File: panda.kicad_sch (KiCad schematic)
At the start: 14 parts

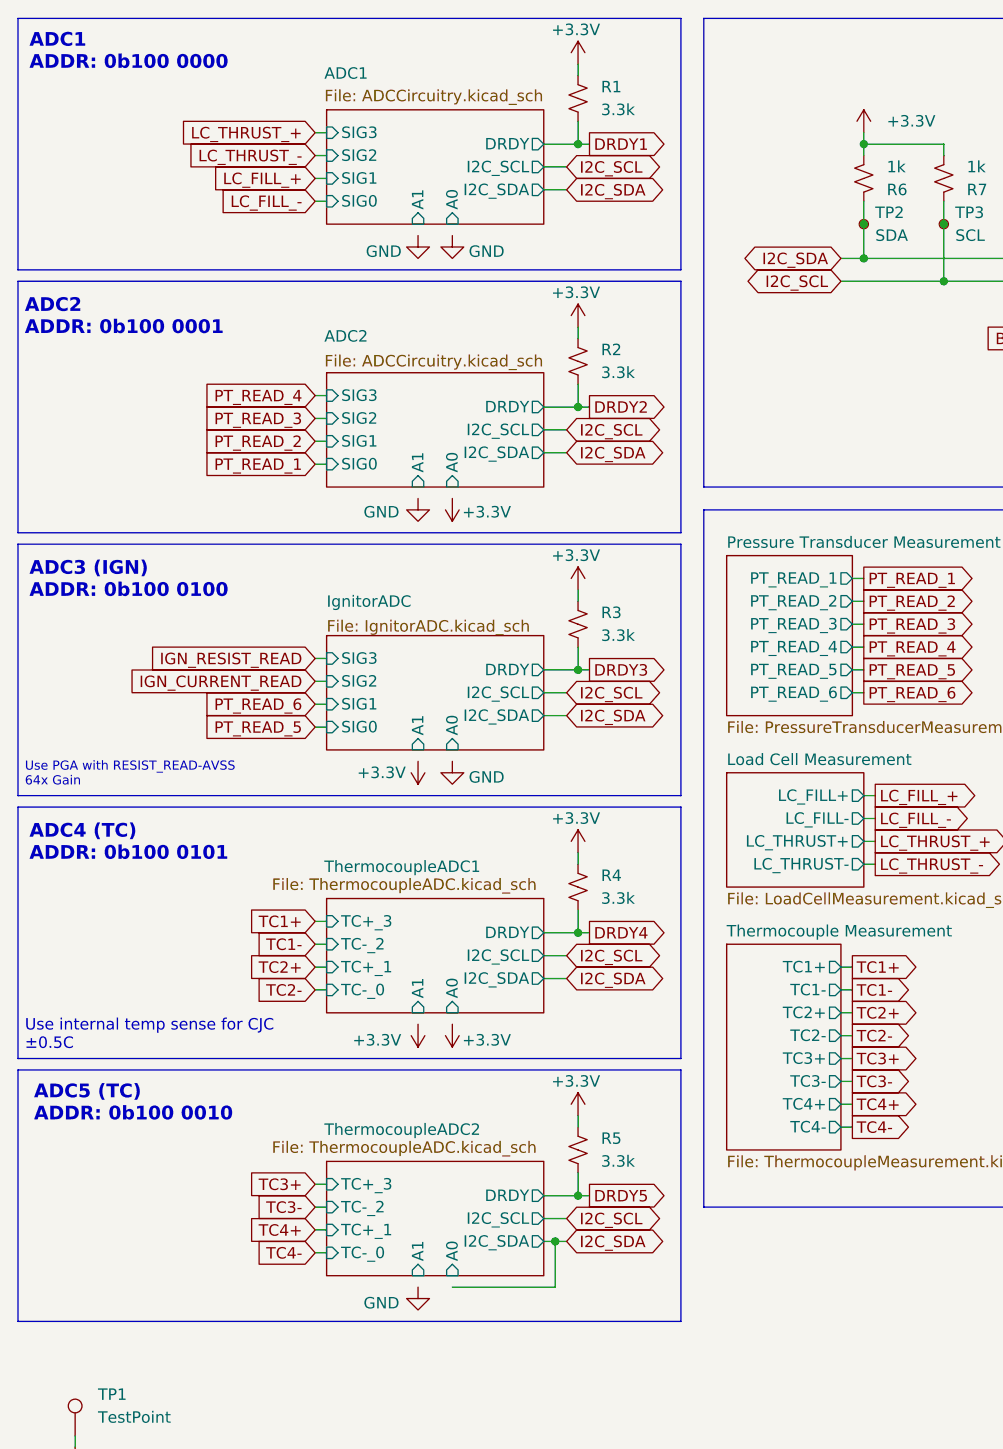
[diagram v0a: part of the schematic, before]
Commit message: change clamping resistors on tc adcs for lower leakage current
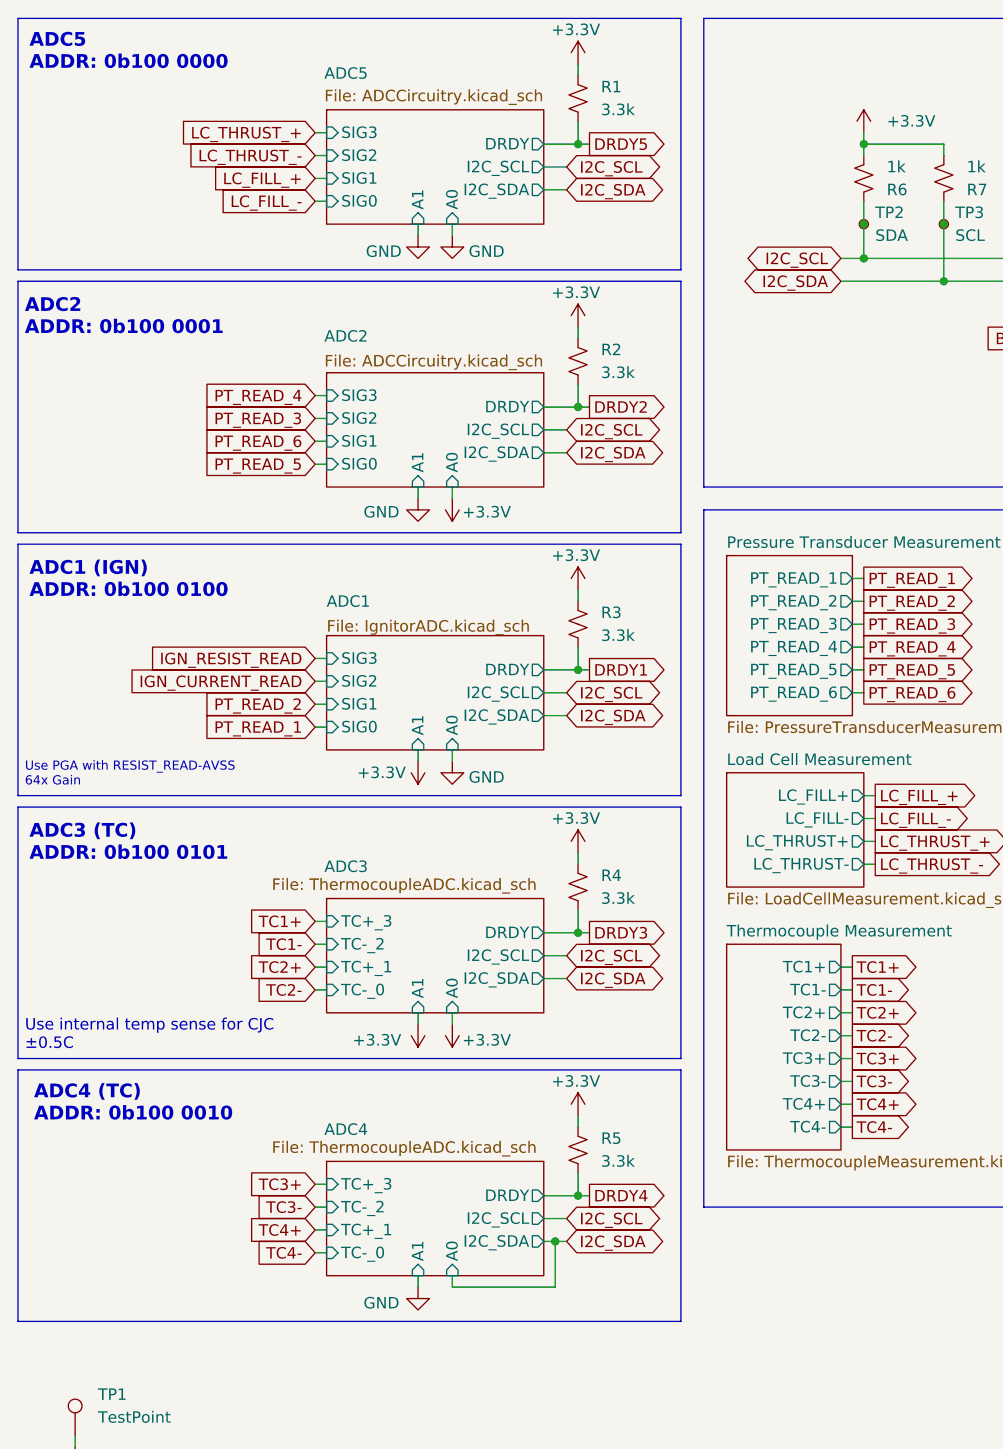
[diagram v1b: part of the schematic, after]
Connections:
- net DRDY1: now also R3.2; no longer R1.2
- net DRDY3: now also R4.2; no longer R3.2
- net DRDY4: now also R5.2; no longer R4.2
- net DRDY5: now also R1.2; no longer R5.2
- net I2C_SCL: now also R6.1, TP2.1; no longer R7.1, TP3.1
- net I2C_SDA: now also R7.1, TP3.1; no longer R6.1, TP2.1
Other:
- sheet ThermocoupleADC1 renamed ADC3
- sheet ThermocoupleADC2 renamed ADC4
- removed sheet IgnitorADC
- added sheet ADC5 (ADCCircuitry.kicad_sch)
- sheet ADC1: file ADCCircuitry.kicad_sch -> IgnitorADC.kicad_sch
- note added: "ADC1 (IGN) ADDR: 0b100 0100"
- note added: "ADC3 (TC) ADDR: 0b100 0101"
- note added: "ADC4 (TC) ADDR: 0b100 0010"
- note added: "ADC5 ADDR: 0b100 0000"
- note removed: "ADC1 ADDR: 0b100 0000"
- note removed: "ADC3 (IGN) ADDR: 0b100 0100"
- note removed: "ADC4 (TC) ADDR: 0b100 0101"
- note removed: "ADC5 (TC) ADDR: 0b100 0010"
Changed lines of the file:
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@@
 		)
 	)
-	(text "ADC3 (IGN)\nADDR: 0b100 0100"
+	(text "ADC1 (IGN)\nADDR: 0b100 0100"
 		(exclude_from_sim no)
 		(at 15.24 76.454 0)
@@
 		)
 	)
-	(text "ADC1\nADDR: 0b100 0000"
+	(text "ADC5\nADDR: 0b100 0000"
 		(exclude_from_sim no)
 		(at 15.24 17.78 0)
@@
 		)
 	)
-	(text "ADC5 (TC)\nADDR: 0b100 0010"
+	(text "ADC4 (TC)\nADDR: 0b100 0010"
 		(exclude_from_sim no)
 		(at 15.748 134.62 0)
@@
 		)
 	)
-	(text "ADC4 (TC)\nADDR: 0b100 0101"
+	(text "ADC3 (TC)\nADDR: 0b100 0101"
 		(exclude_from_sim no)
 		(at 15.24 105.664 0)
@@
 	)
 	(junction
-		(at 116.84 43.18)
-		(diameter 0)
-		(color 0 0 0 0)
-	)
-	(junction
 		(at 76.2 57.15)
 		(diameter 0)
@@
 	)
 	(junction
-		(at 107.95 40.64)
+		(at 116.84 43.18)
 		(diameter 0)
 		(color 0 0 0 0)
@@
 		(color 0 0 0 0)
 	)
+	(junction
+		(at 107.95 40.64)
+		(diameter 0)
+		(color 0 0 0 0)
+	)
 	(wire
 		(pts
@@
 	(wire
 		(pts
+			(xy 58.42 36.83) (xy 58.42 38.1)
+		)
+		(stroke
+			(width 0)
+			(type default)
+		)
+	)
+	(wire
+		(pts
 			(xy 76.2 144.78) (xy 77.47 144.78)
 		)
@@
 	(wire
 		(pts
+			(xy 58.42 66.04) (xy 58.42 67.31)
+		)
+		(stroke
+			(width 0)
+			(type default)
+		)
+	)
+	(wire
+		(pts
 			(xy 105.41 124.46) (xy 106.68 124.46)
 		)
@@
 	(wire
 		(pts
+			(xy 62.23 36.83) (xy 62.23 38.1)
+		)
+		(stroke
+			(width 0)
+			(type default)
+		)
+	)
+	(wire
+		(pts
 			(xy 107.95 107.95) (xy 109.22 107.95)
 		)
@@
 	(wire
 		(pts
-			(xy 46.99 92.71) (xy 48.26 92.71)
+			(xy 58.42 153.67) (xy 58.42 154.94)
 		)
 		(stroke
@@
 	(wire
 		(pts
+			(xy 46.99 92.71) (xy 48.26 92.71)
+		)
+		(stroke
+			(width 0)
+			(type default)
+		)
+	)
+	(wire
+		(pts
 			(xy 72.39 91.44) (xy 74.93 91.44)
 		)
@@
 	(wire
 		(pts
-			(xy 46.99 90.17) (xy 48.26 90.17)
+			(xy 107.95 34.29) (xy 107.95 36.83)
 		)
 		(stroke
@@
 	(wire
 		(pts
-			(xy 107.95 34.29) (xy 107.95 36.83)
+			(xy 46.99 34.29) (xy 48.26 34.29)
 		)
 		(stroke
@@
 	(wire
 		(pts
-			(xy 46.99 34.29) (xy 48.26 34.29)
+			(xy 107.95 100.33) (xy 109.22 100.33)
 		)
 		(stroke
@@
 	(wire
 		(pts
-			(xy 107.95 100.33) (xy 109.22 100.33)
+			(xy 46.99 85.09) (xy 48.26 85.09)
 		)
 		(stroke
@@
 	(wire
 		(pts
-			(xy 46.99 85.09) (xy 48.26 85.09)
+			(xy 107.95 102.87) (xy 109.22 102.87)
 		)
 		(stroke
@@
 	(wire
 		(pts
-			(xy 107.95 102.87) (xy 109.22 102.87)
+			(xy 72.39 59.69) (xy 74.93 59.69)
 		)
 		(stroke
@@
 	(wire
 		(pts
-			(xy 72.39 59.69) (xy 74.93 59.69)
+			(xy 58.42 95.25) (xy 58.42 96.52)
 		)
 		(stroke
@@
 	(wire
 		(pts
+			(xy 62.23 153.67) (xy 62.23 154.94)
+		)
+		(stroke
+			(width 0)
+			(type default)
+		)
+	)
+	(wire
+		(pts
 			(xy 76.2 113.03) (xy 76.2 115.57)
 		)
@@
 	(wire
 		(pts
+			(xy 105.41 43.18) (xy 116.84 43.18)
+		)
+		(stroke
+			(width 0)
+			(type default)
+		)
+	)
+	(wire
+		(pts
 			(xy 46.99 87.63) (xy 48.26 87.63)
 		)
@@
 	(wire
 		(pts
-			(xy 105.41 134.62) (xy 106.68 134.62)
+			(xy 58.42 124.46) (xy 58.42 125.73)
 		)
 		(stroke
@@
 	(wire
 		(pts
-			(xy 46.99 60.96) (xy 48.26 60.96)
+			(xy 105.41 134.62) (xy 106.68 134.62)
 		)
 		(stroke
@@
 	(wire
 		(pts
+			(xy 105.41 40.64) (xy 107.95 40.64)
+		)
+		(stroke
+			(width 0)
+			(type default)
+		)
+	)
+	(wire
+		(pts
 			(xy 46.99 151.13) (xy 48.26 151.13)
 		)
@@
 	(wire
 		(pts
-			(xy 46.99 58.42) (xy 48.26 58.42)
+			(xy 46.99 63.5) (xy 48.26 63.5)
 		)
 		(stroke
@@
 	(wire
 		(pts
-			(xy 105.41 40.64) (xy 107.95 40.64)
+			(xy 72.39 118.11) (xy 74.93 118.11)
 		)
 		(stroke
@@
 	(wire
 		(pts
-			(xy 72.39 118.11) (xy 74.93 118.11)
+			(xy 116.84 34.29) (xy 116.84 36.83)
 		)
 		(stroke
@@
 	(wire
 		(pts
-			(xy 116.84 34.29) (xy 116.84 36.83)
+			(xy 46.99 60.96) (xy 48.26 60.96)
 		)
 		(stroke
@@
 	(wire
 		(pts
+			(xy 62.23 95.25) (xy 62.23 96.52)
+		)
+		(stroke
+			(width 0)
+			(type default)
+		)
+	)
+	(wire
+		(pts
 			(xy 76.2 83.82) (xy 76.2 86.36)
 		)
@@
 	(wire
 		(pts
+			(xy 46.99 58.42) (xy 48.26 58.42)
+		)
+		(stroke
+			(width 0)
+			(type default)
+		)
+	)
+	(wire
+		(pts
 			(xy 105.41 119.38) (xy 106.68 119.38)
 		)
@@
 	(wire
 		(pts
+			(xy 62.23 124.46) (xy 62.23 125.73)
+		)
+		(stroke
+			(width 0)
+			(type default)
+		)
+	)
+	(wire
+		(pts
 			(xy 72.39 27.94) (xy 76.2 27.94)
 		)
@@
 	(wire
 		(pts
-			(xy 46.99 63.5) (xy 48.26 63.5)
+			(xy 62.23 66.04) (xy 62.23 67.31)
 		)
 		(stroke
@@
 	(wire
 		(pts
-			(xy 105.41 43.18) (xy 116.84 43.18)
+			(xy 46.99 146.05) (xy 48.26 146.05)
 		)
 		(stroke
@@
 	(wire
 		(pts
-			(xy 46.99 146.05) (xy 48.26 146.05)
+			(xy 214.63 48.26) (xy 215.9 48.26)
 		)
 		(stroke
@@
 	(wire
 		(pts
-			(xy 214.63 48.26) (xy 215.9 48.26)
+			(xy 72.39 120.65) (xy 74.93 120.65)
 		)
 		(stroke
@@
 	(wire
 		(pts
-			(xy 72.39 120.65) (xy 74.93 120.65)
+			(xy 46.99 90.17) (xy 48.26 90.17)
 		)
 		(stroke
@@
 		)
 	)
-	(global_label "DRDY3"
+	(global_label "DRDY1"
 		(shape output)
 		(at 77.47 86.36 0)
@@
 		)
 	)
-	(global_label "DRDY5"
+	(global_label "DRDY4"
 		(shape output)
 		(at 77.47 144.78 0)
@@
 	(global_label "PT_READ_2"
 		(shape input)
-		(at 46.99 60.96 180)
+		(at 46.99 90.17 180)
 		(fields_autoplaced yes)
 		(effects
@@
 		)
 		(property "Intersheetrefs" "${INTERSHEET_REFS}"
-			(at 33.8449 60.96 0)
+			(at 33.8449 90.17 0)
 			(effects
 				(font
@@
 		)
 	)
-	(global_label "DRDY4"
+	(global_label "DRDY3"
 		(shape output)
 		(at 77.47 115.57 0)
@@
 	(global_label "PT_READ_1"
 		(shape input)
-		(at 46.99 63.5 180)
+		(at 46.99 92.71 180)
 		(fields_autoplaced yes)
 		(effects
@@
 		)
 		(property "Intersheetrefs" "${INTERSHEET_REFS}"
-			(at 33.8449 63.5 0)
+			(at 33.8449 92.71 0)
 			(effects
 				(font
@@
 		)
 	)
-	(global_label "DRDY1"
+	(global_label "DRDY5"
 		(shape output)
 		(at 77.47 27.94 0)
@@
 	(global_label "I2C_SDA"
 		(shape bidirectional)
-		(at 105.41 40.64 180)
+		(at 105.41 43.18 180)
 		(fields_autoplaced yes)
 		(effects
@@
 		)
 		(property "Intersheetrefs" "${INTERSHEET_REFS}"
-			(at 93.6935 40.64 0)
+			(at 93.6935 43.18 0)
 			(effects
 				(font
@@
 	(global_label "I2C_SCL"
 		(shape bidirectional)
-		(at 105.41 43.18 180)
+		(at 105.41 40.64 180)
 		(fields_autoplaced yes)
 		(effects
@@
 		)
 		(property "Intersheetrefs" "${INTERSHEET_REFS}"
-			(at 93.754 43.18 0)
+			(at 93.754 40.64 0)
 			(effects
 				(font
@@
 	(global_label "PT_READ_5"
 		(shape input)
-		(at 46.99 92.71 180)
+		(at 46.99 63.5 180)
 		(fields_autoplaced yes)
 		(effects
@@
 		)
 		(property "Intersheetrefs" "${INTERSHEET_REFS}"
-			(at 33.8449 92.71 0)
+			(at 33.8449 63.5 0)
 			(effects
 				(font
@@
 	(global_label "PT_READ_6"
 		(shape input)
-		(at 46.99 90.17 180)
+		(at 46.99 60.96 180)
 		(fields_autoplaced yes)
 		(effects
@@
 		)
 		(property "Intersheetrefs" "${INTERSHEET_REFS}"
-			(at 33.8449 90.17 0)
+			(at 33.8449 60.96 0)
 			(effects
 				(font
@@
 			(color 0 0 0 0.0000)
 		)
-		(property "Sheetname" "ADC1"
+		(property "Sheetname" "ADC5"
 			(at 48.006 20.828 0)
 			(effects
@@
 			(color 0 0 0 0.0000)
 		)
-		(property "Sheetname" "ThermocoupleADC2"
+		(property "Sheetname" "ADC4"
 			(at 48.006 138.176 0)
 			(effects
@@
 			(color 0 0 0 0.0000)
 		)
-		(property "Sheetname" "ThermocoupleADC1"
+		(property "Sheetname" "ADC3"
 			(at 48.006 108.966 0)
 			(effects
@@
 			(color 0 0 0 0.0000)
 		)
-		(property "Sheetname" "IgnitorADC"
+		(property "Sheetname" "ADC1"
 			(at 48.26 79.502 0)
 			(effects

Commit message: Update version number in KiCad files
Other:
- title: (none) -> PANDA
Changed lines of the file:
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@@
 	(paper "A4")
 	(title_block
-		(rev "1.0.0")
+		(title "PANDA")
+		(date "2025-12-21")
+		(rev "3.0.0")
 		(company "Queen's Rocket Engineering Team")
+		(comment 1 "Propulsion Actuation and Data Acquisition")
 	)
 	(rectangle

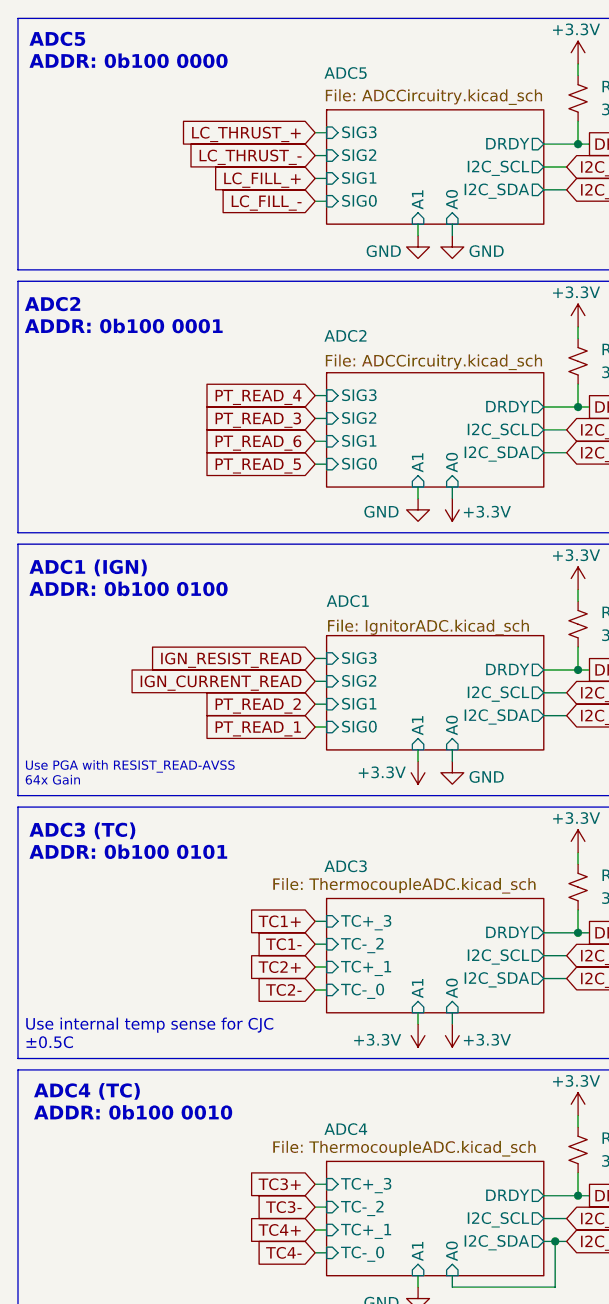
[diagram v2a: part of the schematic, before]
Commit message: fix adc numbering on schematic
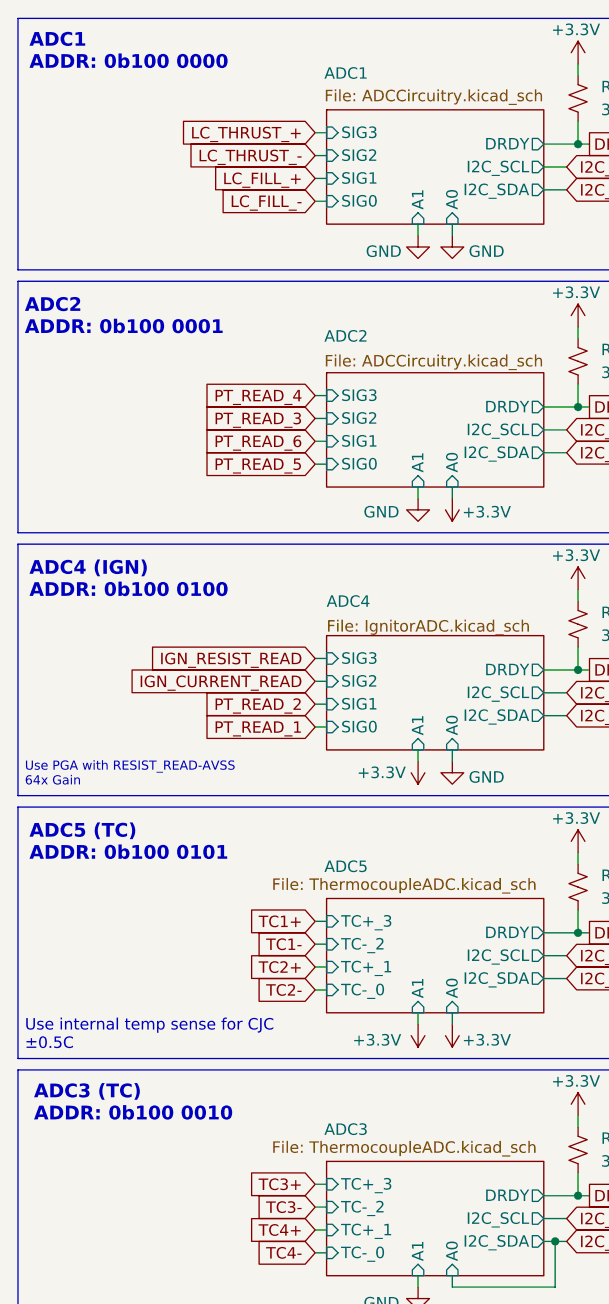
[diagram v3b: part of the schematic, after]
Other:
- sheet ADC1: file IgnitorADC.kicad_sch -> ADCCircuitry.kicad_sch
- sheet ADC4: file ThermocoupleADC.kicad_sch -> IgnitorADC.kicad_sch
- sheet ADC4 ports: added SIG0, SIG1, SIG2, SIG3; removed TC+_1, TC+_3, TC-_0, TC-_2
- sheet ADC5: file ADCCircuitry.kicad_sch -> ThermocoupleADC.kicad_sch
- sheet ADC5 ports: added TC+_1, TC+_3, TC-_0, TC-_2; removed SIG0, SIG1, SIG2, SIG3
- note added: "ADC1 ADDR: 0b100 0000"
- note added: "ADC3 (TC) ADDR: 0b100 0010"
- note added: "ADC4 (IGN) ADDR: 0b100 0100"
- note added: "ADC5 (TC) ADDR: 0b100 0101"
- note removed: "ADC1 (IGN) ADDR: 0b100 0100"
- note removed: "ADC3 (TC) ADDR: 0b100 0101"
- note removed: "ADC4 (TC) ADDR: 0b100 0010"
- note removed: "ADC5 ADDR: 0b100 0000"
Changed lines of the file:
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@@
 		)
 	)
-	(text "ADC1 (IGN)\nADDR: 0b100 0100"
+	(text "ADC4 (IGN)\nADDR: 0b100 0100"
 		(exclude_from_sim no)
 		(at 15.24 76.454 0)
@@
 		)
 	)
-	(text "ADC5\nADDR: 0b100 0000"
+	(text "ADC1\nADDR: 0b100 0000"
 		(exclude_from_sim no)
 		(at 15.24 17.78 0)
@@
 		)
 	)
-	(text "ADC4 (TC)\nADDR: 0b100 0010"
+	(text "ADC3 (TC)\nADDR: 0b100 0010"
 		(exclude_from_sim no)
 		(at 15.748 134.62 0)
@@
 		)
 	)
-	(text "ADC3 (TC)\nADDR: 0b100 0101"
+	(text "ADC5 (TC)\nADDR: 0b100 0101"
 		(exclude_from_sim no)
 		(at 15.24 105.664 0)
@@
 			(color 0 0 0 0.0000)
 		)
-		(property "Sheetname" "ADC5"
+		(property "Sheetname" "ADC1"
 			(at 48.006 20.828 0)
 			(effects
@@
 			(color 0 0 0 0.0000)
 		)
-		(property "Sheetname" "ADC4"
+		(property "Sheetname" "ADC3"
 			(at 48.006 138.176 0)
 			(effects
@@
 			(color 0 0 0 0.0000)
 		)
-		(property "Sheetname" "ADC3"
+		(property "Sheetname" "ADC5"
 			(at 48.006 108.966 0)
 			(effects
@@
 			(color 0 0 0 0.0000)
 		)
-		(property "Sheetname" "ADC1"
+		(property "Sheetname" "ADC4"
 			(at 48.26 79.502 0)
 			(effects
